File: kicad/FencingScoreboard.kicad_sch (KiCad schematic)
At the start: 20 parts, among them IC1 PIC16F18855-I-ML, IC2 STP16CPC26, IC3 STP16CPC26, J1 USB_B_Micro, J2 Conn_01x03_Pin, J3 Conn_01x03_Pin, Q1 2N7002

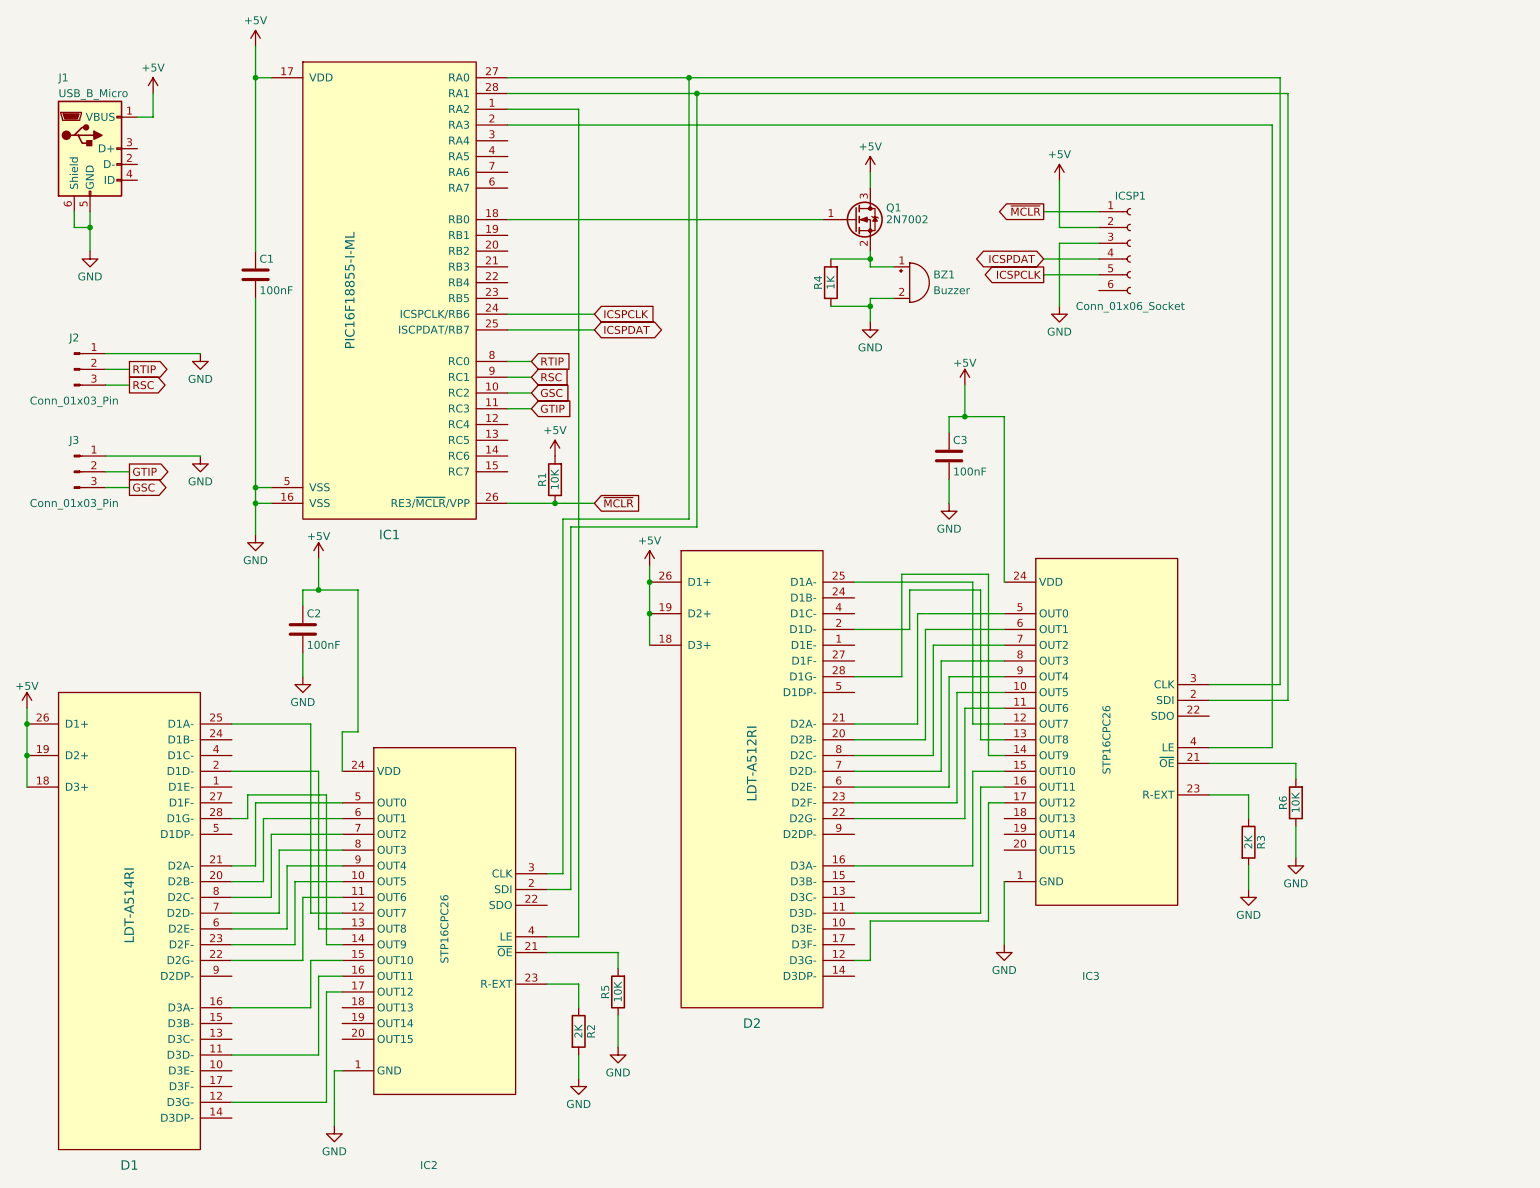
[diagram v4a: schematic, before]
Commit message: Correct for PPS port restrictions, schematic cleanup
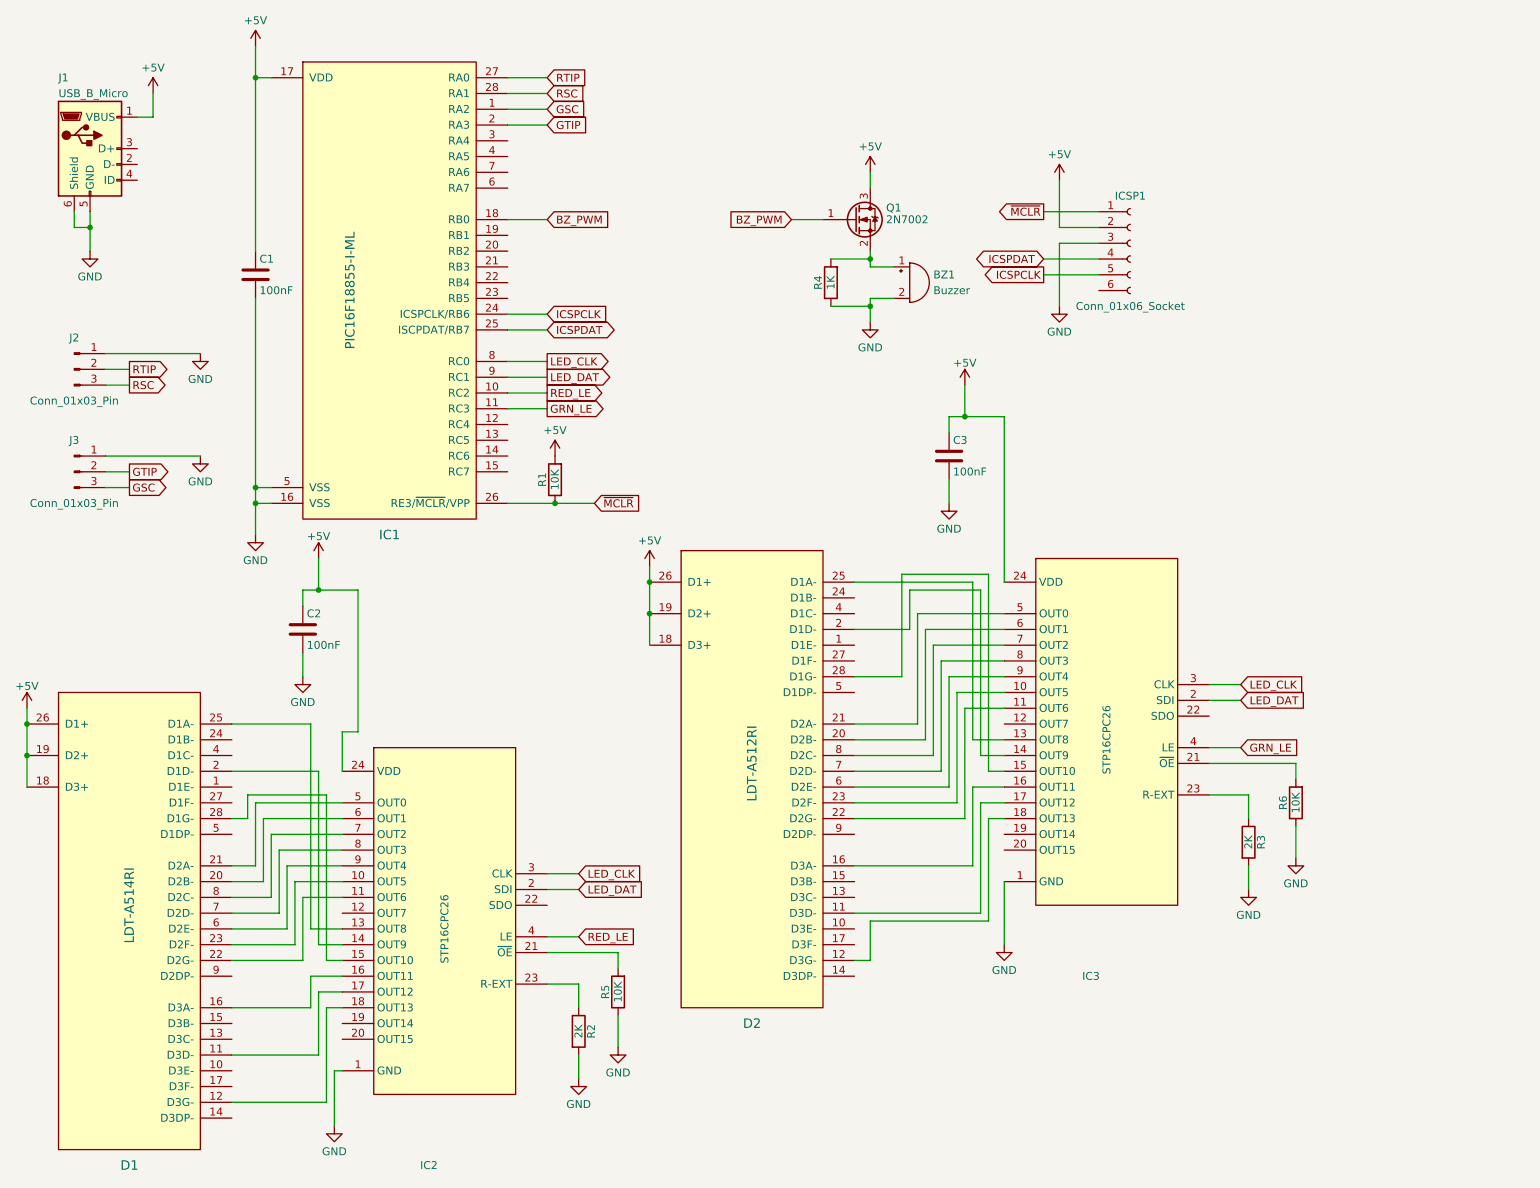
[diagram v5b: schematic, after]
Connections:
- net GSC: now also IC1.1 (RA2); no longer IC1.10 (RC2)
- net GTIP: now also IC1.2 (RA3); no longer IC1.11 (RC3)
- net RSC: now also IC1.28 (RA1); no longer IC1.9 (RC1)
- net RTIP: now also IC1.27 (RA0); no longer IC1.8 (RC0)
- net at D2.11 (D3D-): now also IC3.17 (OUT12); no longer IC3.16 (OUT11)
- net at D2.12 (D3G-): now also IC3.18 (OUT13); no longer IC3.17 (OUT12)
- net at D2.16 (D3A-): now also IC3.16 (OUT11); no longer IC3.15 (OUT10)
- net at D2.2 (D1D-): now also IC3.14 (OUT9); no longer IC3.13 (OUT8)
- net at D2.25 (D1A-): now also IC3.13 (OUT8); no longer IC3.12 (OUT7)
- net at D2.28 (D1G-): now also IC3.15 (OUT10); no longer IC3.14 (OUT9)
- net at D1.11 (D3D-): now also IC2.17 (OUT12); no longer IC2.16 (OUT11)
- net at D1.12 (D3G-): now also IC2.18 (OUT13); no longer IC2.17 (OUT12)
- net at D1.16 (D3A-): now also IC2.16 (OUT11); no longer IC2.15 (OUT10)
- net at D1.2 (D1D-): now also IC2.14 (OUT9); no longer IC2.13 (OUT8)
- net at D1.25 (D1A-): now also IC2.13 (OUT8); no longer IC2.12 (OUT7)
- net at D1.28 (D1G-): now also IC2.15 (OUT10); no longer IC2.14 (OUT9)
- net LED_DAT: now reaches IC2.2 (SDI), IC3.2 (SDI)
- net LED_DAT: now also IC1.9 (RC1); no longer IC1.28 (RA1)
- net LED_CLK: now reaches IC2.3 (CLK), IC3.3 (CLK)
- net LED_CLK: now also IC1.8 (RC0); no longer IC1.27 (RA0)
- net RED_LE: now reaches IC2.4 (LE)
- net RED_LE: now also IC1.10 (RC2); no longer IC1.1 (RA2)
- net GRN_LE: now reaches IC3.4 (LE)
- net GRN_LE: now also IC1.11 (RC3); no longer IC1.2 (RA3)
- net BZ_PWM: now reaches IC1.18 (RB0), Q1.1 (G)

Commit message: Schematic cleanup, start PCB re-route
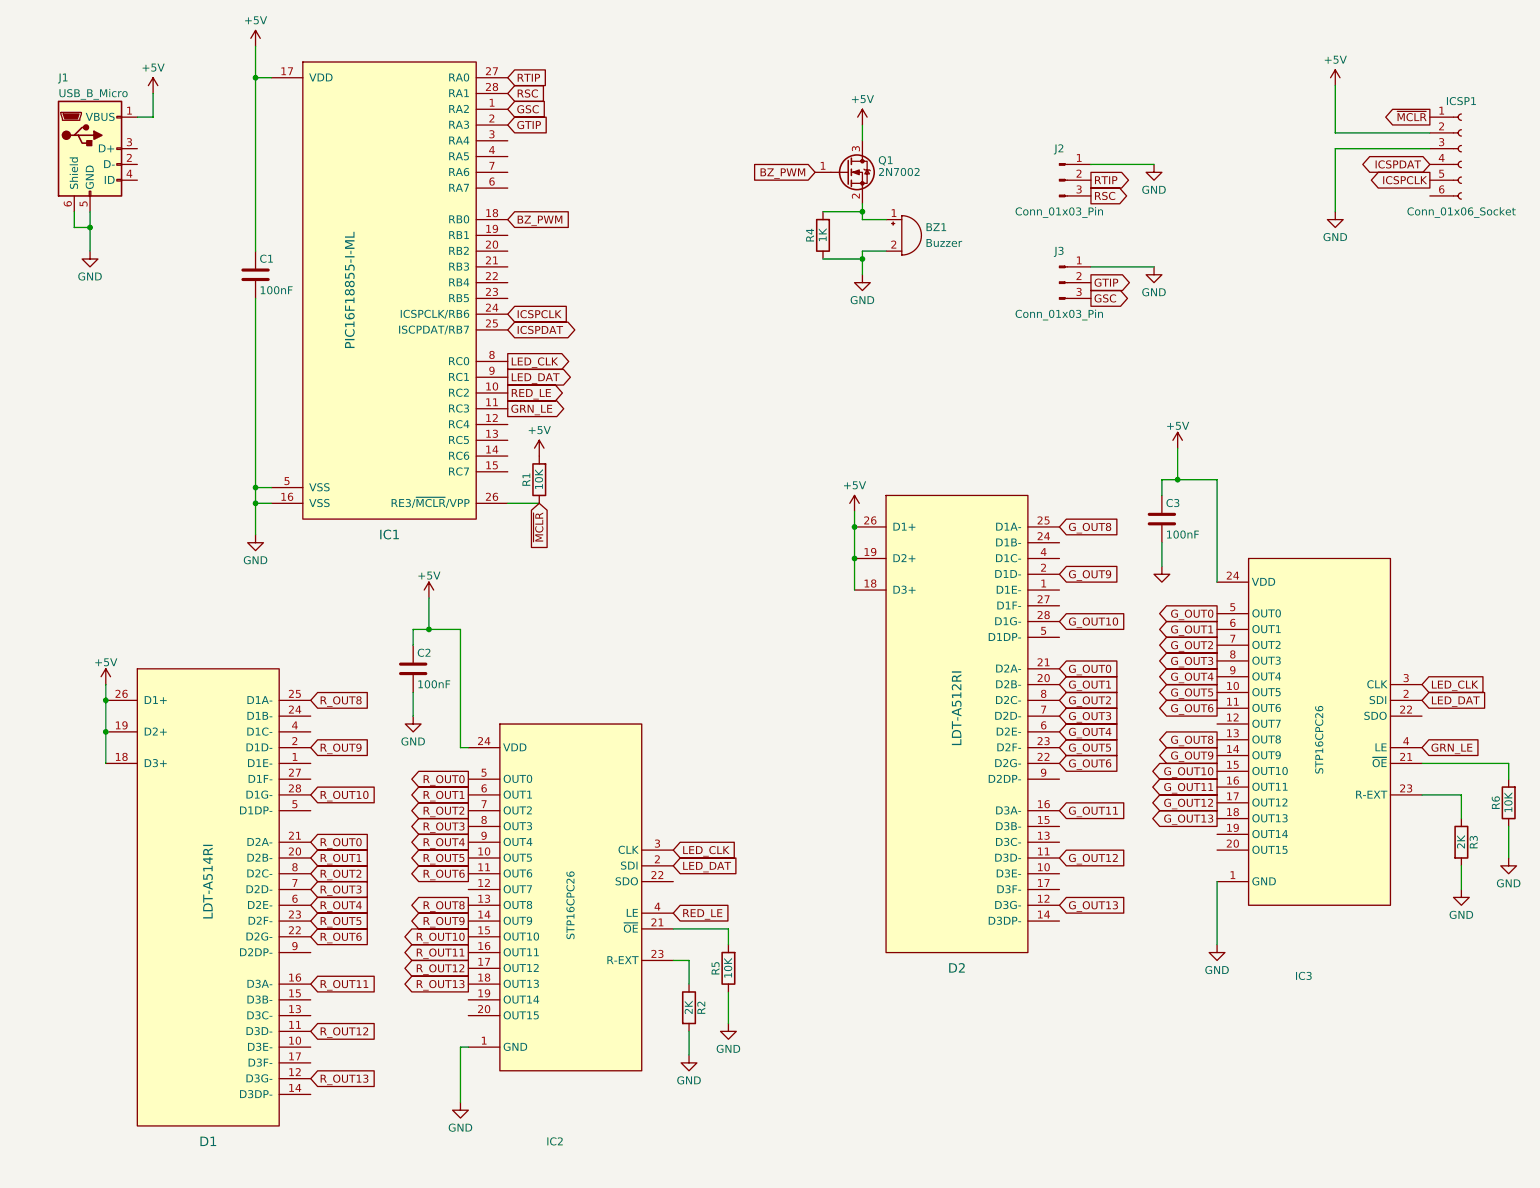
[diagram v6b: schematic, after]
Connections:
- net G_OUT12: now reaches D2.11 (D3D-), IC3.17 (OUT12)
- net G_OUT13: now reaches D2.12 (D3G-), IC3.18 (OUT13)
- net G_OUT11: now reaches D2.16 (D3A-), IC3.16 (OUT11)
- net G_OUT9: now reaches D2.2 (D1D-), IC3.14 (OUT9)
- net G_OUT1: now reaches D2.20 (D2B-), IC3.6 (OUT1)
- net G_OUT0: now reaches D2.21 (D2A-), IC3.5 (OUT0)
- net G_OUT6: now reaches D2.22 (D2G-), IC3.11 (OUT6)
- net G_OUT5: now reaches D2.23 (D2F-), IC3.10 (OUT5)
- net G_OUT8: now reaches D2.25 (D1A-), IC3.13 (OUT8)
- net G_OUT10: now reaches D2.28 (D1G-), IC3.15 (OUT10)
- net G_OUT4: now reaches D2.6 (D2E-), IC3.9 (OUT4)
- net G_OUT3: now reaches D2.7 (D2D-), IC3.8 (OUT3)
- net G_OUT2: now reaches D2.8 (D2C-), IC3.7 (OUT2)
- net R_OUT12: now reaches D1.11 (D3D-), IC2.17 (OUT12)
- net R_OUT13: now reaches D1.12 (D3G-), IC2.18 (OUT13)
- net R_OUT11: now reaches D1.16 (D3A-), IC2.16 (OUT11)
- net R_OUT9: now reaches D1.2 (D1D-), IC2.14 (OUT9)
- net R_OUT1: now reaches D1.20 (D2B-), IC2.6 (OUT1)
- net R_OUT0: now reaches D1.21 (D2A-), IC2.5 (OUT0)
- net R_OUT6: now reaches D1.22 (D2G-), IC2.11 (OUT6)
- net R_OUT5: now reaches D1.23 (D2F-), IC2.10 (OUT5)
- net R_OUT8: now reaches D1.25 (D1A-), IC2.13 (OUT8)
- net R_OUT10: now reaches D1.28 (D1G-), IC2.15 (OUT10)
- net R_OUT4: now reaches D1.6 (D2E-), IC2.9 (OUT4)
- net R_OUT3: now reaches D1.7 (D2D-), IC2.8 (OUT3)
- net R_OUT2: now reaches D1.8 (D2C-), IC2.7 (OUT2)
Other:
- moved on the sheet: BZ1, C2, C3, D1, D2, IC2, IC3, ICSP1, J2, J3, Q1, R1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

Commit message: Update J2, J3, BZ1 footprints
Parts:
- BZ1: footprint Buzzer_Beeper:Buzzer_12x9.5RM7.6 -> Buzzer_Beeper:MagneticBuzzer_ProSignal_ABT-410-RC
- J2, J3: footprint Connector_PinHeader_1.27mm:PinHeader_1x03_P1.27mm_Vertical -> Connector_PinHeader_2.54mm:PinHeader_1x03_P2.54mm_Vertical
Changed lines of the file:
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@@
   (title_block
     (title "Fencing Hit Indicator with Score Display")
-    (date "2024-01-17")
-    (rev "A")
+    (date "2024-01-24")
+    (rev "B")
     (company "David's MakerWorks")
     (comment 1 "github.com/davidsmakerworks")
@@
       (effects (font (size 1.27 1.27)))
     )
-    (property "Footprint" "Connector_PinHeader_1.27mm:PinHeader_1x03_P1.27mm_Vertical" (at 187.96 57.15 0)
+    (property "Footprint" "Connector_PinHeader_2.54mm:PinHeader_1x03_P2.54mm_Vertical" (at 187.96 57.15 0)
       (effects (font (size 1.27 1.27)) hide)
     )
@@
       (effects (font (size 1.27 1.27)) (justify left))
     )
-    (property "Footprint" "Buzzer_Beeper:Buzzer_12x9.5RM7.6" (at 161.925 46.99 90)
+    (property "Footprint" "Buzzer_Beeper:MagneticBuzzer_ProSignal_ABT-410-RC" (at 161.925 46.99 90)
       (effects (font (size 1.27 1.27)) hide)
     )
@@
       (effects (font (size 1.27 1.27)))
     )
-    (property "Footprint" "Connector_PinHeader_1.27mm:PinHeader_1x03_P1.27mm_Vertical" (at 187.96 40.64 0)
-      (effects (font (size 1.27 1.27)) hide)
-    )
+    (property "Footprint" "Connector_PinHeader_2.54mm:PinHeader_1x03_P2.54mm_Vertical" (at 187.96 40.64 0)
+      (effects (font (size 1.27 1.27)) hide)
+    )
